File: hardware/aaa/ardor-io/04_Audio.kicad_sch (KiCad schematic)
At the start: 15 parts, among them U401 OPA2320AIDR, U402 OPA2320AIDR

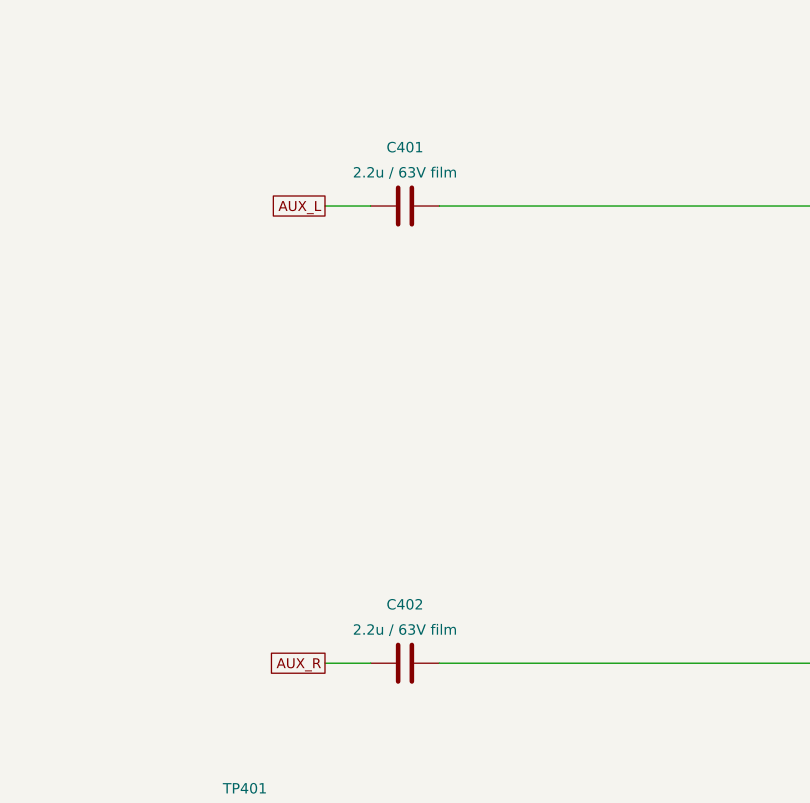
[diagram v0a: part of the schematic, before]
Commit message: feat: smd capacitors
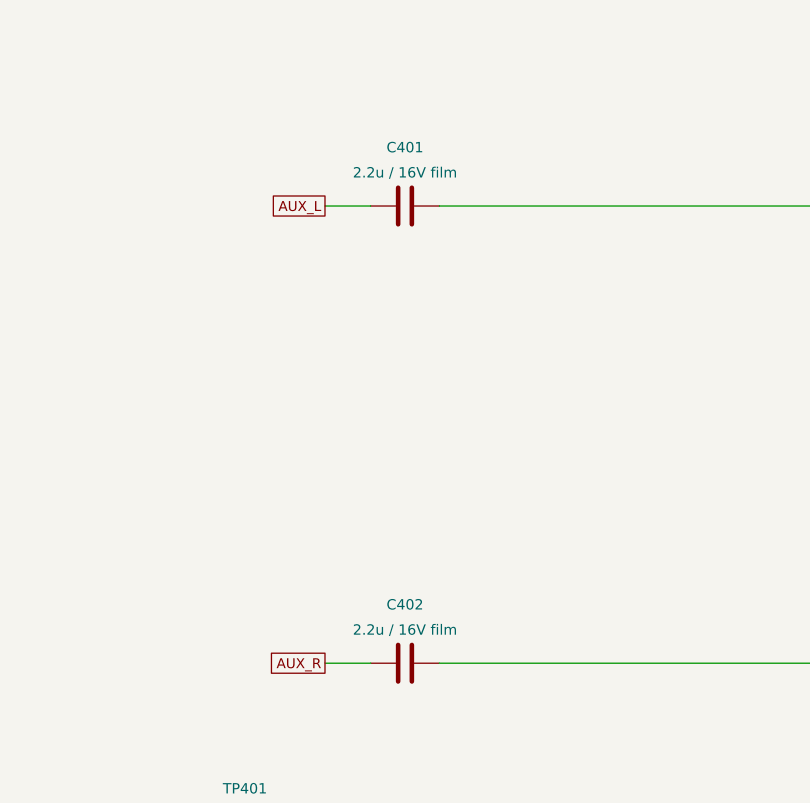
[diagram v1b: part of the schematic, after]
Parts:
- C401, C402: value 2.2u / 63V film -> 2.2u / 16V film; footprint Capacitor_THT:C_Rect_L7.2mm_W7.2mm_P5.00mm_FKS2_FKP2_MKS2_MKP2 -> Ardor_Capacitor:C_Rubycon_MU_3225; MPN WIMA MKS2C042201K00KSSD -> Rubycon 16MU225KB23225

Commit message: feat: update Ardor IO PCB for hardware rev2
- Update schematics, routing, BOM, and design documentation
- Add SMD capacitor conversion and verification tooling
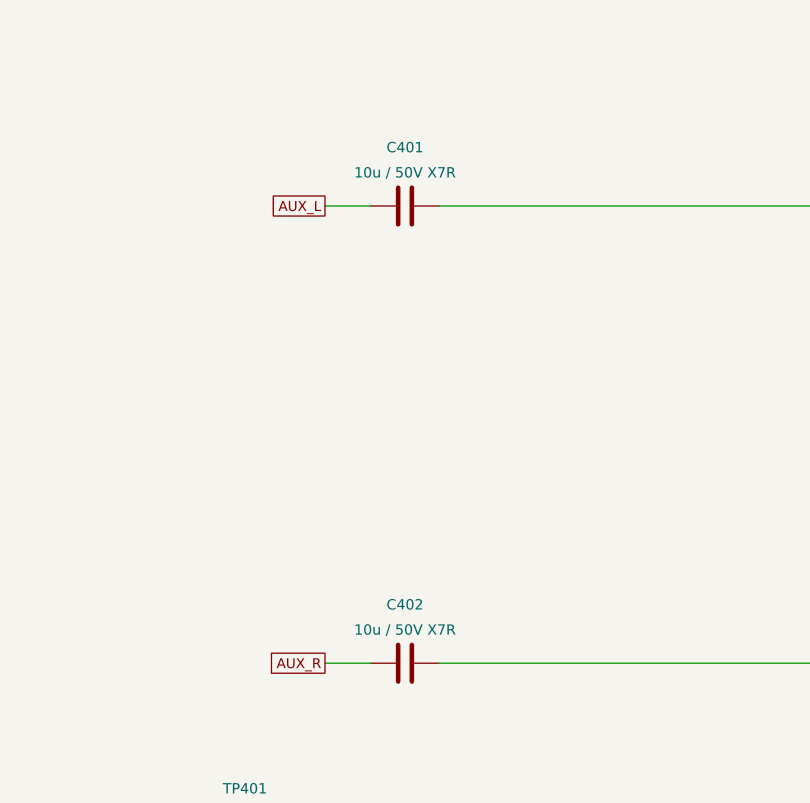
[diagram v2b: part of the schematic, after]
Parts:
- C401, C402: value 2.2u / 16V film -> 10u / 50V X7R; footprint Ardor_Capacitor:C_Rubycon_MU_3225 -> Capacitor_SMD:C_1206_3216Metric; JLCPCB Part # (none) -> C89632; MPN Rubycon 16MU225KB23225 -> Samsung CL31B106KBHNNNE

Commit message: feat: finalize Ardor IO hardware rev2 production package
- Update schematics, PCB, BOM, and documentation
- Add assembly exports, review artifacts, and verification data
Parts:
- C403: value 10u / 10V X7R -> 10u / 16V X7R; JLCPCB Part # (none) -> C95841; MPN (none) -> Samsung CL21B106KOQNNNE
- C404, C405: value 100n / 16V -> 100n / 50V X7R; JLCPCB Part # (none) -> C14663; MPN (none) -> YAGEO CC0603KRX7R9BB104
- R401, R402: JLCPCB Part # (none) -> C25803; MPN (none) -> UNI-ROYAL 0603WAF1003T5E
- R403, R404: JLCPCB Part # (none) -> C95204; MPN (none) -> YAGEO RT0603BRD0710KL
- R405, R406: JLCPCB Part # (none) -> C25804; MPN (none) -> UNI-ROYAL 0603WAF1002T5E
- U401, U402: JLCPCB Part # (none) -> C2863402
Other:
- note added: "Nominal audio target <=1.0 Vrms per AUX channel. Unity gain throughout. OPA2320: RRIO on 5 V, unity stable; 2.5 V bias permits bipolar audio swing. 10u/100k input pole ~0.159 Hz. Keep VREF local; no large capacitor directly on buffer output."
- note removed: "Nominal audio target <=1.0 Vrms per AUX channel. Unity gain throughout. OPA2320: RRIO on 5 V, unity stable; 2.5 V bias permits bipolar audio swing. 2.2u/100k input pole ~0.72 Hz. Keep VREF local; no large capacitor directly on buffer output."
